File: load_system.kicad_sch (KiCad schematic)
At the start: 0 parts

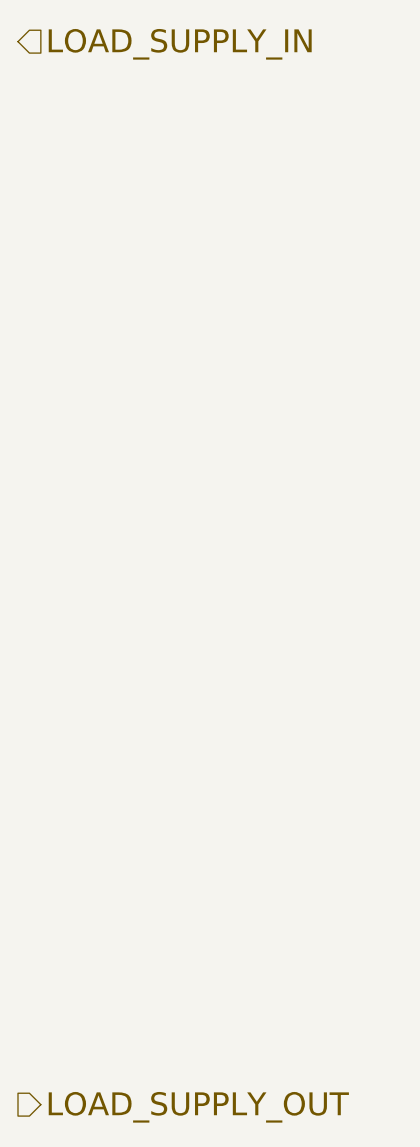
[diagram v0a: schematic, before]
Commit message: fix:fixed hall sensor connections
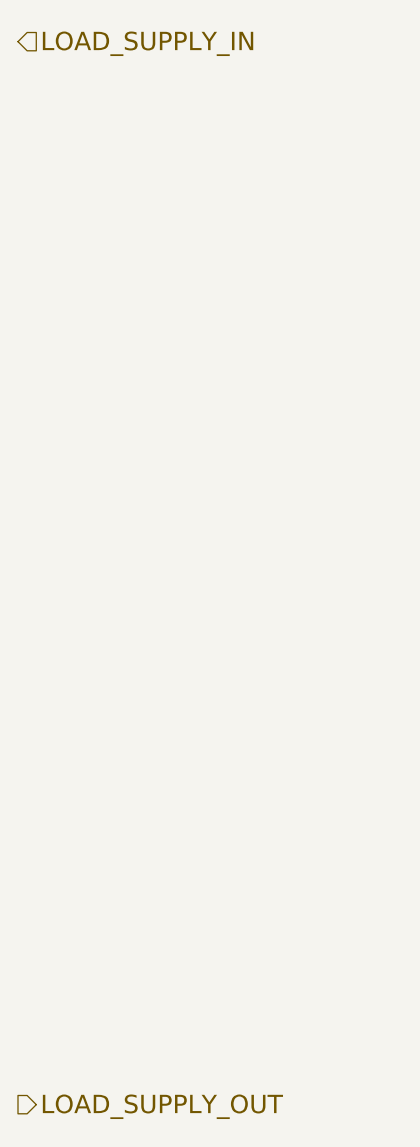
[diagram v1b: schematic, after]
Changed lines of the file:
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@@
 		(effects
 			(font
-				(size 2.54 2.54)
+				(size 2.032 2.032)
 			)
 			(justify left)
@@
 		(effects
 			(font
-				(size 2.54 2.54)
+				(size 2.032 2.032)
 			)
 			(justify left)
